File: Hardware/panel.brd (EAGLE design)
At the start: 79 x 43 mm, 86 parts, among them Q1 BC817-40LT1SMD, Q10 BC807-16LT1SMD, Q11 BC807-16LT1SMD, Q12 BC807-16LT1SMD, Q13 BC817-40LT1SMD, Q14 BC817-40LT1SMD, Q15 BC817-40LT1SMD, Q16 BC817-40LT1SMD, Q17 BC817-40LT1SMD, Q18 BC817-40LT1SMD, Q19 BC817-40LT1SMD, Q2 BC817-40LT1SMD, Q3 BC817-40LT1SMD, Q4 BC817-40LT1SMD, Q5 BC817-40LT1SMD, Q6 BC807-16LT1SMD, Q7 BC807-16LT1SMD, Q8 BC807-16LT1SMD, Q9 BC807-16LT1SMD, U1 MC7805CDT, X1 B16B-PHDSS, X2 52746-20

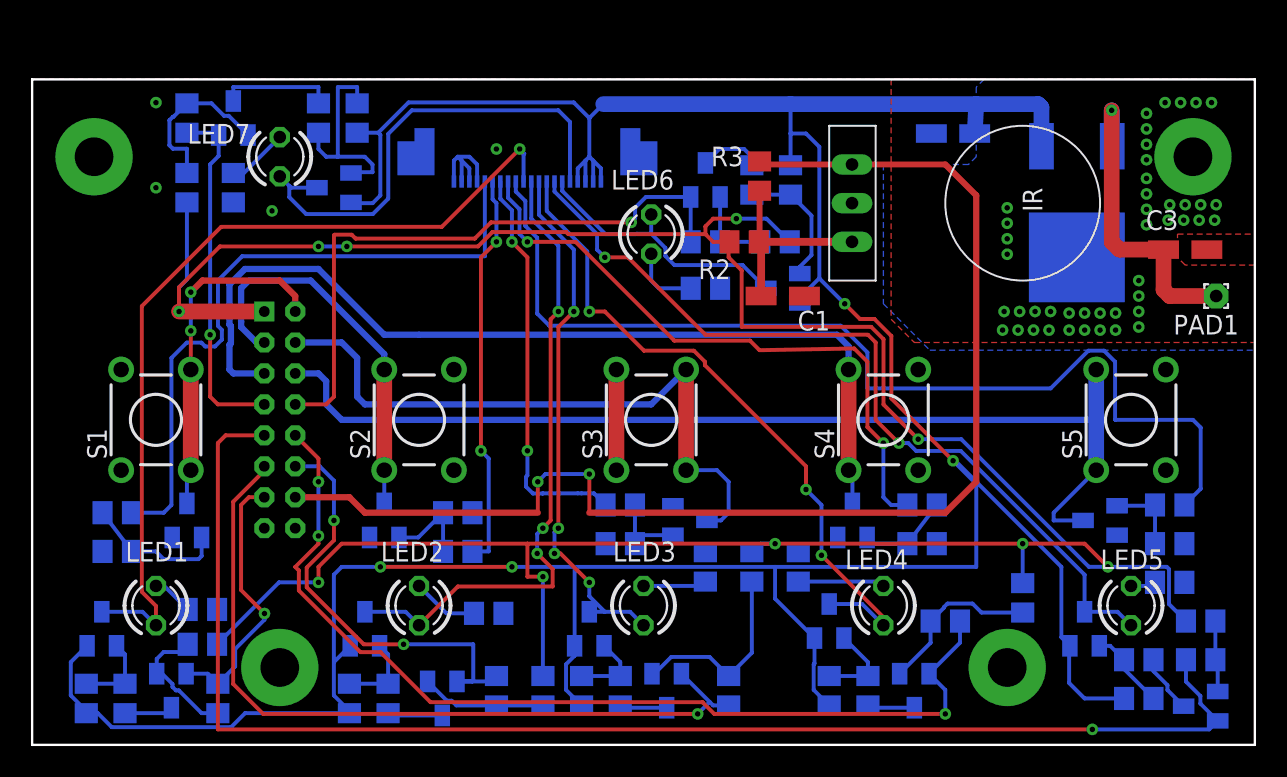
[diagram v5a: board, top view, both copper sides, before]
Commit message: оставил только часть с индикатором и переразвел ее под макетную плату
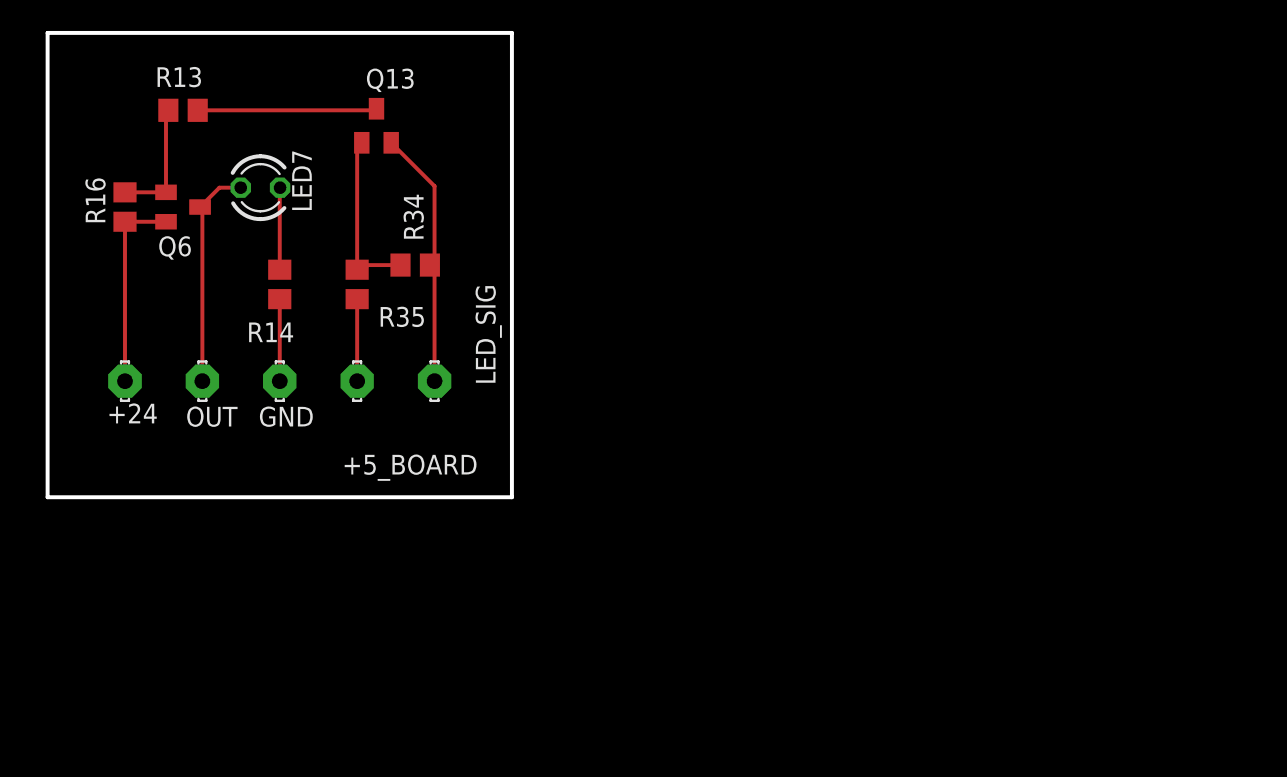
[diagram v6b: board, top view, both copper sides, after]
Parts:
- removed C1: 10uF 16v, rcl:CT3216
- removed C2: 0.33uF, rcl:CT3216
- removed C3: 0.1uF, rcl:CT3216
- removed LED1: red, led_user:LED_RED_3MM
- removed LED2, LED3, LED4, LED5, LED6: green, led_user:LED_GREEN_3MM
- removed PAD1: (no value), wirepad:1,6/0,8
- removed Q1, Q14, Q15, Q16, Q17, Q18, Q19, Q2, Q3, Q4, Q5: BC817-40LT1SMD, transistor-npn:SOT23-BEC
- removed Q10, Q11, Q12, Q7, Q8, Q9: BC807-16LT1SMD, transistor-pnp_user:SOT23
- removed R1, R10, R11, R12, R15, R18, R19, R21, R22, R24, R25, R27, R28, R30, R31, R33, R36, R38, R4, R40, R42, R44, R46, R5, R6, R7, R8, R9: 4.7k, rcl:R0805
- removed R17, R20, R23, R26, R29, R32: 2.2k, rcl:R0805
- removed R2: 51, rcl:R0805
- removed R3: 15k, rcl:R0805
- removed R37, R39, R41, R43, R45, R47: 800, rcl:R0805
- removed S1, S2, S3, S4, S5: 7mm, switch_user:TL1105F
- removed U$1: TSOP4838FLAT, tsop:HDRVR14W64P250_1X14_2266X508X754B
- removed U1: MC7805CDT, _hhn_78xx_79xx_NCV78xx_d2pak_dpak:DPAK-3
- removed X1: B16B-PHDSS, con-JST PHD:B16B-PHDSS
- removed X2: 52746-20, con-molex_user:52746-20
- added +24, +5_BOARD, GND, LED_SIG, OUT: LSP10, solpad:LSP10
- moved R34 17.5 mm to (23.8, 30.0), flipped to the top, turned to 0 degrees
- moved R16 16.1 mm to (5.00, 33.8), flipped to the top
- moved R35 12.7 mm to (20.0, 28.8), flipped to the top
- moved Q6 9.83 mm to (8.75, 33.8), flipped to the top
- moved Q13 9.26 mm to (21.2, 39.0), flipped to the top
- moved R13 8.76 mm to (8.75, 40.0), flipped to the top, turned to 0 degrees
- moved R14 6.93 mm to (15.0, 28.8), flipped to the top
- moved LED7 2.36 mm to (13.8, 35.0), turned to 0 degrees
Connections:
- removed net ADJLED: Q18.E, R44.2, X1.12
- removed net ADJLED_SIG: LED2.A, Q9.3, X2.11
- removed net DOWNLED: Q17.E, R42.2, X1.11
- removed net DOWNLED_SIG: LED3.A, Q10.3, X2.12
- removed net FFSW: Q5.C, S5.1, S5.3, X1.6
- removed net FF_SIG: R12.2, X2.9
- removed net FNSW: Q4.C, S4.1, S4.3, X1.5
- removed net FN_SIG: R10.2, X2.8
- removed net IR: R3.1, U$1.OUT, X1.14
- removed net LASERSW: Q3.C, S3.2, S3.4, X1.4
- removed net LASER_SIG: R8.2, X2.7
- removed net N$1: Q1.B, R1.2, R4.1
- removed net N$11: Q14.B, R36.1, R37.2
- removed net N$12: Q7.1, R15.1, R18.1
- removed net N$13: LED6.K, R17.2
- removed net N$14: Q8.1, R19.1, R21.1
- removed net N$15: LED1.K, R20.2
- removed net N$16: Q9.1, R22.1, R24.1
- removed net N$17: LED2.K, R23.2
- removed net N$18: Q10.1, R25.1, R27.1
- removed net N$19: LED3.K, R26.2
- removed net N$2: C1.+, R2.1, R3.2, U$1.VCC
- removed net N$20: Q11.1, R28.1, R30.1
- removed net N$21: LED4.K, R29.2
- removed net N$22: Q12.1, R31.1, R33.1
- removed net N$23: LED5.K, R32.2
- removed net N$25: Q14.C, R15.2
- removed net N$26: Q15.B, R38.1, R39.2
- removed net N$27: Q15.C, R31.2
- removed net N$28: Q16.B, R40.1, R41.2
- removed net N$29: Q16.C, R28.2
- removed net N$30: Q17.B, R42.1, R43.2
- removed net N$31: Q17.C, R25.2
- removed net N$32: Q18.B, R44.1, R45.2
- removed net N$33: Q18.C, R22.2
- removed net N$34: Q19.B, R46.1, R47.2
- removed net N$35: Q19.C, R19.2
- removed net N$4: Q2.B, R5.2, R6.1
- removed net N$5: Q3.B, R7.2, R8.1
- removed net N$6: Q4.B, R10.1, R9.2
- removed net N$7: Q5.B, R11.2, R12.1
- removed net PRW_SIG: R4.2, X2.5
- removed net PWRLED: Q19.E, R46.2, X1.13
- removed net PWRLED_SIG: LED1.A, Q8.3, X2.10
- removed net PWR_SW: Q1.C, S1.2, S1.4, X1.2
- removed net SETSW: Q2.C, S2.1, S2.3, X1.3
- removed net SET_SIG: R6.2, X2.6
- removed net UPLED: Q14.E, R36.2, X1.8
- removed net UPLED_SIG: LED6.A, Q7.3, X2.15
- removed net VOUT_SB: C3.+, PAD1.1, U1.3
- removed net XLED: Q16.E, R40.2, X1.10
- removed net XLED_SIG: LED4.A, Q11.3, X2.13
- removed net YLED: Q15.E, R38.2, X1.9
- removed net YLED_SIG: LED5.A, Q12.3, X2.14
- net +24V: now also +24.MP; no longer C2.+, Q10.2, Q11.2, Q12.2, Q7.2, Q8.2, Q9.2, R18.2, R21.2, R24.2, R27.2, R30.2, R33.2, U1.1, X2.17, X2.18, X2.19, X2.20
- net +5V: now also +5_BOARD.MP; no longer R2.2, R37.1, R39.1, R41.1, R43.1, R45.1, R47.1, X1.1
- net GND: now also GND.MP; no longer C1.-, C2.-, C3.-, Q1.E, Q2.E, Q3.E, Q4.E, Q5.E, R1.1, R11.1, R17.1, R20.1, R23.1, R26.1, R29.1, R32.1, R5.1, R7.1, R9.1, S1.1, S1.3, S2.2, S2.4, S3.1, S3.3, S4.2, S4.4, S5.2, S5.4, U$1.GND, U1.4, X1.15, X1.16, X2.1, X2.2, X2.3, X2.4
- net LVLED: now also LED_SIG.MP; no longer X1.7
- net LVLLED_SIG: now also OUT.MP; no longer X2.16
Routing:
- net +24V: track 222.9 -> 12.9 mm, vias 4 -> 0
- net +5V: track 179.9 -> 5.30 mm, vias 10 -> 0
- net YLED: track 91.3 -> 0.00 mm, vias 1 -> 0
- net IR: track 83.3 -> 0.00 mm, vias 2 -> 0
- net FFSW: track 66.7 -> 0.00 mm
- net FF_SIG: track 66.0 -> 0.00 mm
- net XLED: track 63.7 -> 0.00 mm, vias 3 -> 0
- net FNSW: track 60.7 -> 0.00 mm
- net PWRLED_SIG: track 55.7 -> 0.00 mm, vias 1 -> 0
- net YLED_SIG: track 54.4 -> 0.00 mm, vias 2 -> 0
- net DOWNLED: track 50.7 -> 0.00 mm, vias 1 -> 0
- net XLED_SIG: track 44.2 -> 0.00 mm, vias 3 -> 0
- net PRW_SIG: track 42.9 -> 0.00 mm
- net LASERSW: track 42.5 -> 0.00 mm
- net ADJLED_SIG: track 41.4 -> 0.00 mm, vias 3 -> 0
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- removed copper zone on layer 1, net GND
- removed copper zone on layer 16, net GND
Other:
- board size 79 x 43 mm -> 30 x 30 mm

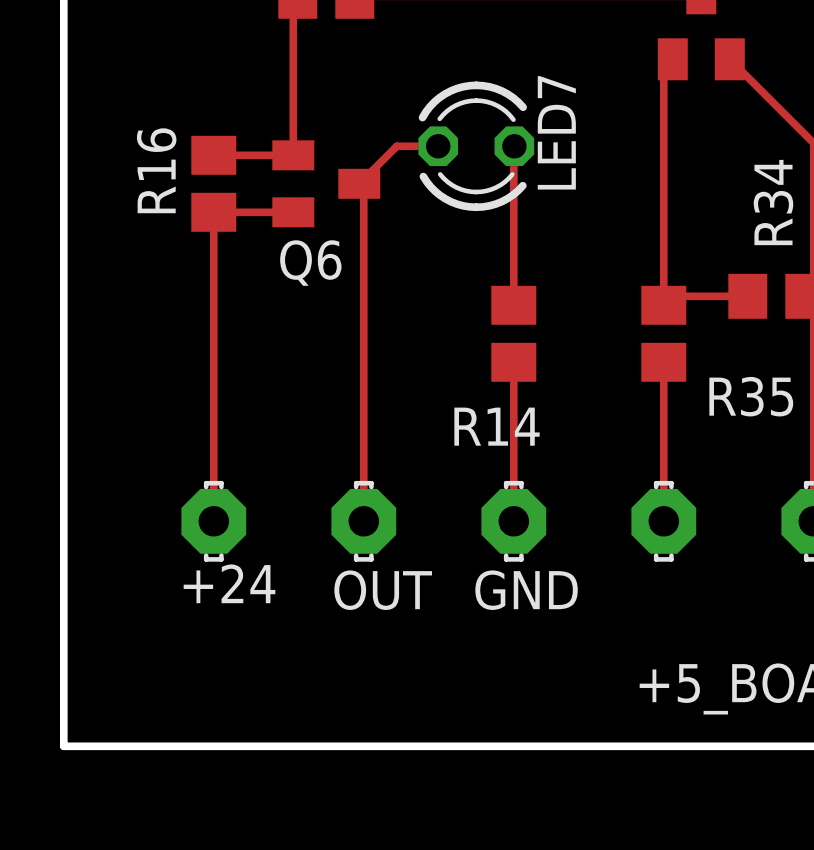
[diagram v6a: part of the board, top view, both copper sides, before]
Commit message: проверил работоспособность решения. нес защитный резистор от закоротки выхода на землю, чтоб не сгорал транзистор
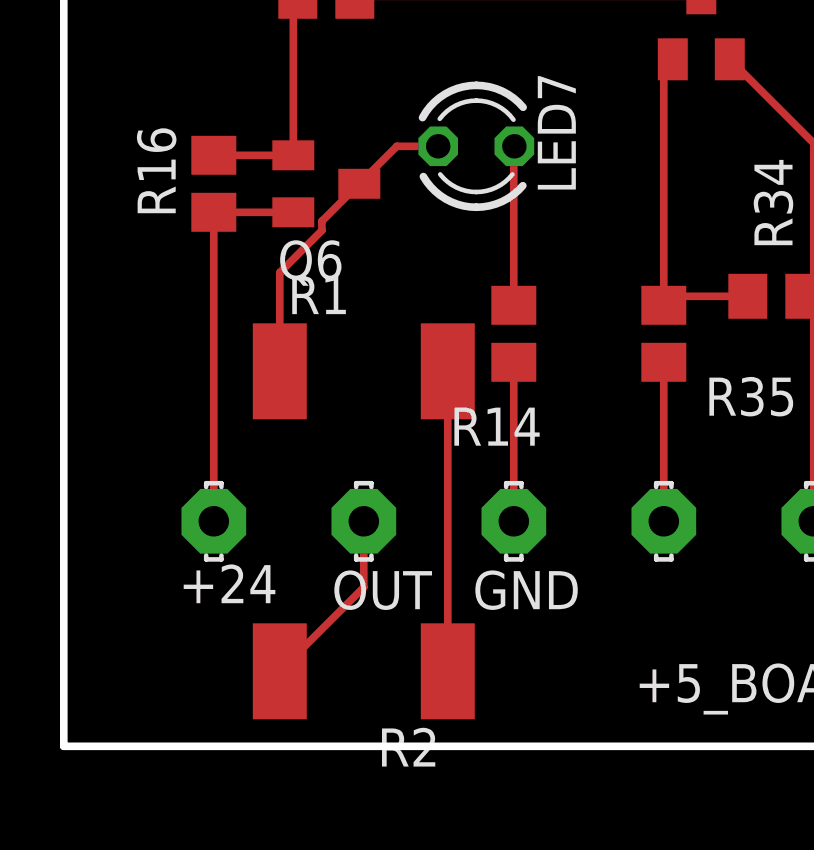
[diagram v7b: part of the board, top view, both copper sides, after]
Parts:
- added R1, R2: 150, rcl:R2512
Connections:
- new net N$1: R1.2, R2.1
- new net N$2: OUT.MP, R2.2
- net LVLLED_SIG: now also R1.1; no longer OUT.MP
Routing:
- net N$1: track 0.00 -> 10.4 mm
- net N$2: track 0.00 -> 6.16 mm
- net LVLLED_SIG: track 14.5 -> 10.7 mm
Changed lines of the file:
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@@
 <attribute name="VALUE" x="15.254" y="22.5" size="0.0254" layer="27" rot="R270"/>
+</element>
+<element name="R1" library="rcl" library_urn="urn:adsk.eagle:library:334" package="R2512" package3d_urn="urn:adsk.eagle:package:23545/2" value="150" x="10" y="27.5" smashed="yes">
+<attribute name="NAME" x="7.46" y="29.405" size="1.27" layer="25"/>
+<attribute name="POPULARITY" value="0" x="10" y="27.5" size="1.778" layer="27" display="off"/>
+<attribute name="SPICEPREFIX" value="R" x="10" y="27.5" size="1.778" layer="27" display="off"/>
+<attribute name="VALUE" x="7.46" y="24.325" size="1.27" layer="27"/>
+</element>
+<element name="R2" library="rcl" library_urn="urn:adsk.eagle:library:334" package="R2512" package3d_urn="urn:adsk.eagle:package:23545/2" value="150" x="10" y="17.5" smashed="yes" rot="R180">
+<attribute name="NAME" x="12.54" y="15.595" size="1.27" layer="25" rot="R180"/>
+<attribute name="POPULARITY" value="0" x="10" y="17.5" size="1.778" layer="27" rot="R180" display="off"/>
+<attribute name="SPICEPREFIX" value="R" x="10" y="17.5" size="1.778" layer="27" rot="R180" display="off"/>
+<attribute name="VALUE" x="12.54" y="20.675" size="1.27" layer="27" rot="R180"/>
 </element>
 </elements>
@@
 <contactref element="Q6" pad="3"/>
 <contactref element="LED7" pad="A"/>
-<contactref element="OUT" pad="MP"/>
-<wire x1="10" y1="22.5" x2="10" y2="33.6" width="0.254" layer="1"/>
 <wire x1="10" y1="33.6" x2="9.85" y2="33.75" width="0.254" layer="1"/>
 <wire x1="9.85" y1="33.75" x2="11.1" y2="35" width="0.254" layer="1"/>
 <wire x1="11.1" y1="35" x2="12.48" y2="35" width="0.254" layer="1"/>
+<contactref element="R1" pad="1"/>
+<wire x1="9.85" y1="33.75" x2="8.604" y2="32.504" width="0.254" layer="1"/>
+<wire x1="8.604" y1="32.504" x2="8.604" y2="32.1947875" width="0.254" layer="1"/>
+<wire x1="7.2" y1="30.7907875" x2="7.2" y2="27.5" width="0.254" layer="1"/>
+<wire x1="8.604" y1="32.1947875" x2="7.2" y2="30.7907875" width="0.254" layer="1"/>
 </signal>
 <signal name="N$10">
@@
 <wire x1="21.15" y1="40" x2="9.7" y2="40" width="0.254" layer="1"/>
 </signal>
+<signal name="N$1">
+<contactref element="R1" pad="2"/>
+<contactref element="R2" pad="1"/>
+<wire x1="12.8" y1="27.5" x2="12.8" y2="17.8" width="0.254" layer="1"/>
+<wire x1="12.8" y1="17.8" x2="12.5" y2="17.5" width="0.254" layer="1"/>
+<wire x1="12.5" y1="17.5" x2="12.8" y2="17.5" width="0.254" layer="1"/>
+</signal>
+<signal name="N$2">
+<contactref element="OUT" pad="MP"/>
+<contactref element="R2" pad="2"/>
+<wire x1="7.2" y1="17.5" x2="10" y2="20.3" width="0.254" layer="1"/>
+<wire x1="10" y1="20.3" x2="10" y2="22.5" width="0.254" layer="1"/>
+</signal>
 </signals>
